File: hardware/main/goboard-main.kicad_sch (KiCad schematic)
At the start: 15 parts, among them J1 USB_C_Receptacle_USB2.0, J2 Conn_02x05_Top_Bottom, J3 Conn_01x01, J4 Conn_01x05, SW11 SW_Push, SW30 SW_DP3T

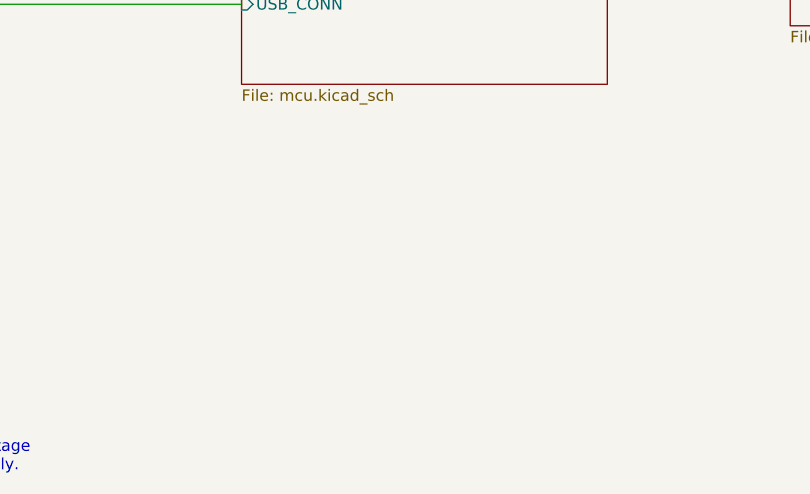
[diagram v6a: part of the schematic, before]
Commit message: Add the USB sense circuit to the PCB
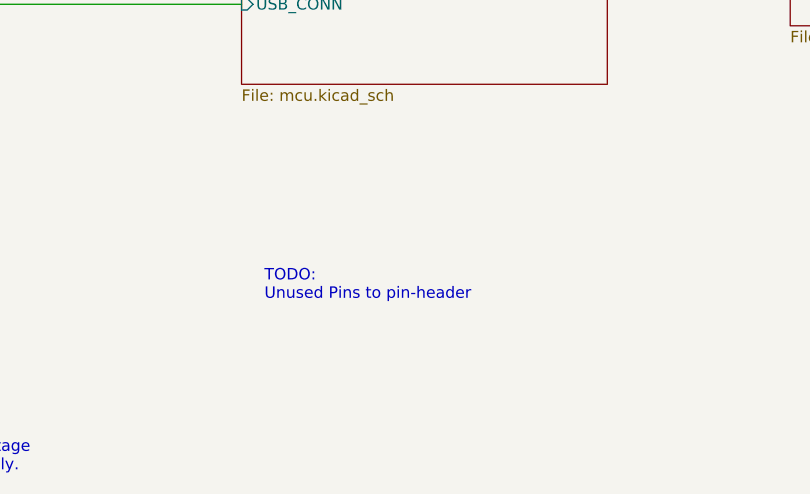
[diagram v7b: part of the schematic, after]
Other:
- note added: "TODO: Unused Pins to pin-header"
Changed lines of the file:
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@@
+    (effects (font (size 1.27 1.27)) (justify left bottom))
+  )
+  (text "TODO:\nUnused Pins to pin-header" (at 123.19 177.8 0)
     (effects (font (size 1.27 1.27)) (justify left bottom))
   )
@@
       (reference "#PWR0140") (unit 1) (value "GND") (footprint "")
     )
+    (path "/a2ebbcc0-d455-4794-9fcf-d50cef56d65b/94c3f1f0-9419-428a-a6f7-165b4feb93a2"
+      (reference "#PWR0141") (unit 1) (value "+3.3V") (footprint "")
+    )
     (path "/a2ebbcc0-d455-4794-9fcf-d50cef56d65b/5a4b2b5e-200b-4d68-9e34-c2caa68d1a58"
-      (reference "#PWR?") (unit 1) (value "GND") (footprint "")
-    )
-    (path "/a2ebbcc0-d455-4794-9fcf-d50cef56d65b/94c3f1f0-9419-428a-a6f7-165b4feb93a2"
-      (reference "#PWR?") (unit 1) (value "+3.3V") (footprint "")
+      (reference "#PWR0150") (unit 1) (value "GND") (footprint "")
     )
     (path "/a2ebbcc0-d455-4794-9fcf-d50cef56d65b/210515f0-c0f1-4f80-b920-f3ce9df10676"
@@
     )
     (path "/a2ebbcc0-d455-4794-9fcf-d50cef56d65b/c7d4bd51-d701-4c56-9708-a98feca559b8"
-      (reference "Q?") (unit 1) (value "BC817") (footprint "Package_TO_SOT_SMD:SOT-23")
+      (reference "Q11") (unit 1) (value "BC817") (footprint "Package_TO_SOT_SMD:SOT-23")
     )
     (path "/a2ebbcc0-d455-4794-9fcf-d50cef56d65b/94b1480c-21b6-4ef7-b592-3977ba8ffc39"
@@
       (reference "R29") (unit 1) (value "10K") (footprint "Resistor_SMD:R_0603_1608Metric")
     )
+    (path "/a2ebbcc0-d455-4794-9fcf-d50cef56d65b/f6e90b97-7f06-4011-bca1-7aebee2af537"
+      (reference "R30") (unit 1) (value "4.7K") (footprint "Resistor_SMD:R_0603_1608Metric")
+    )
     (path "/a2ebbcc0-d455-4794-9fcf-d50cef56d65b/02993b3e-bd6a-4b6e-8520-b01ae08d0060"
-      (reference "R?") (unit 1) (value "10K") (footprint "Resistor_SMD:R_0603_1608Metric")
-    )
-    (path "/a2ebbcc0-d455-4794-9fcf-d50cef56d65b/f6e90b97-7f06-4011-bca1-7aebee2af537"
-      (reference "R?") (unit 1) (value "4.7K") (footprint "Resistor_SMD:R_0603_1608Metric")
+      (reference "R31") (unit 1) (value "10K") (footprint "Resistor_SMD:R_0603_1608Metric")
     )
     (path "/a2ebbcc0-d455-4794-9fcf-d50cef56d65b/fa148395-83b6-415a-8f1a-6bb3d54e1164"
